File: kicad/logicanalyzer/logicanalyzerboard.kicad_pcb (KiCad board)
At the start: 4 copper layers, 100 x 100 mm, 46 parts, among them J1 Conn_01x06, J2 Conn_02x32_Odd_Even, J3 Conn_01x02, J5 USB_B_Micro, J6 Conn_01x02, SW1 SW_Push, U1 XC6SLX9-TQG144, U3 W25Q32JVSS, U4 SN74LVC16245ADGGR, U5 SN74LVC16245ADGGR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

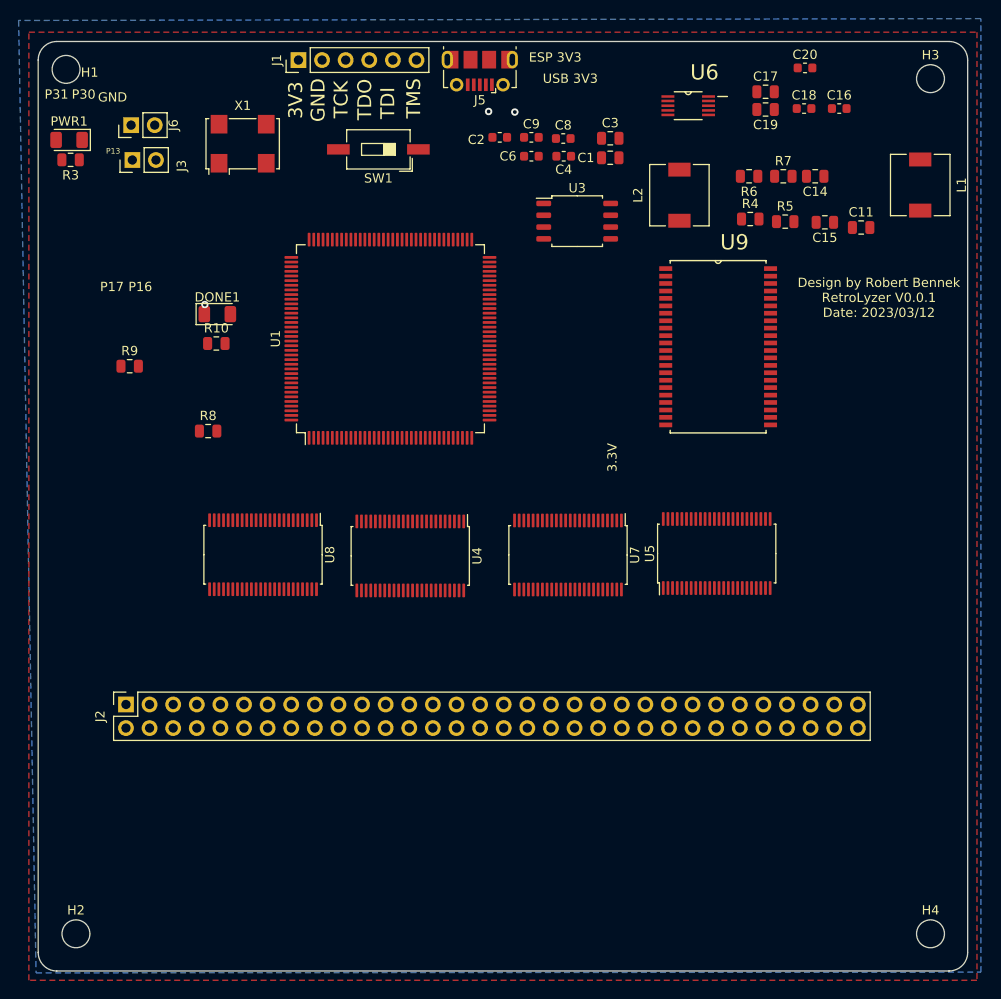
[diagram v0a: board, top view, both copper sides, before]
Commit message: #1 now also the logic board too
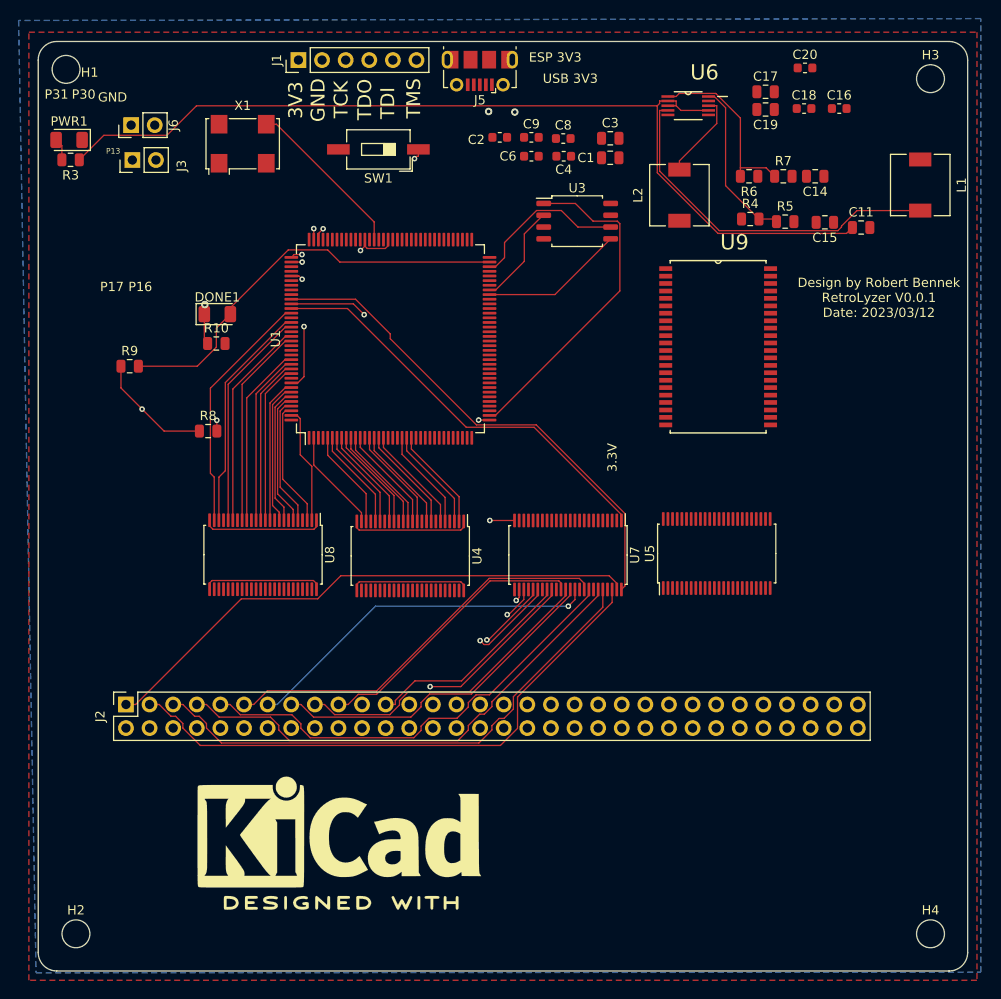
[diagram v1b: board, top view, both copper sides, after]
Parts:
- added REF**: KiCad-Logo2_12mm_SilkScreen, Symbol:KiCad-Logo2_12mm_SilkScreen, F.Cu at (132.4, 115.0)
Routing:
- net +5V: track 0.00 -> 103.2 mm
- net A2: track 0.00 -> 61.6 mm
- net Net-(U1C-PROGRAM_B_2): track 0.00 -> 60.0 mm, vias 0 -> 3
- net A1: track 0.00 -> 59.5 mm
- net A3: track 0.00 -> 57.2 mm
- net /FPGA/nOE_3_1: track 0.00 -> 54.1 mm
- net A4: track 0.00 -> 52.8 mm
- net A5: track 0.00 -> 48.9 mm
- net /FPGA/DIR_3_1: track 0.00 -> 45.3 mm
- net /FPGA/FPGA_DONE: track 0.00 -> 45.1 mm
- net A6: track 0.00 -> 43.1 mm
- net Net-(U6-SW1): track 0.00 -> 39.1 mm
- net A7: track 0.00 -> 38.8 mm, vias 0 -> 1
- net /FPGA/DIR_3_2: track 0.00 -> 38.7 mm, vias 0 -> 2
- net A8: track 0.00 -> 36.9 mm
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
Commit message: #1 refreshed logic board image
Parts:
- moved REF** 2.30 mm to (130.3, 116.1)
- turned U5 to -90 degrees
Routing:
- net +1V2: track 0.00 -> 2.22 mm, vias 2 -> 3
